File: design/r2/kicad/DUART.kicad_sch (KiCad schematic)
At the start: 17 parts, among them IC4 XR68C681CJTR-F, J1 UART_A, J2 UART_B, J4 Conn_01x06, J7 Conn_01x01_Male, Q1 3.6864MHz

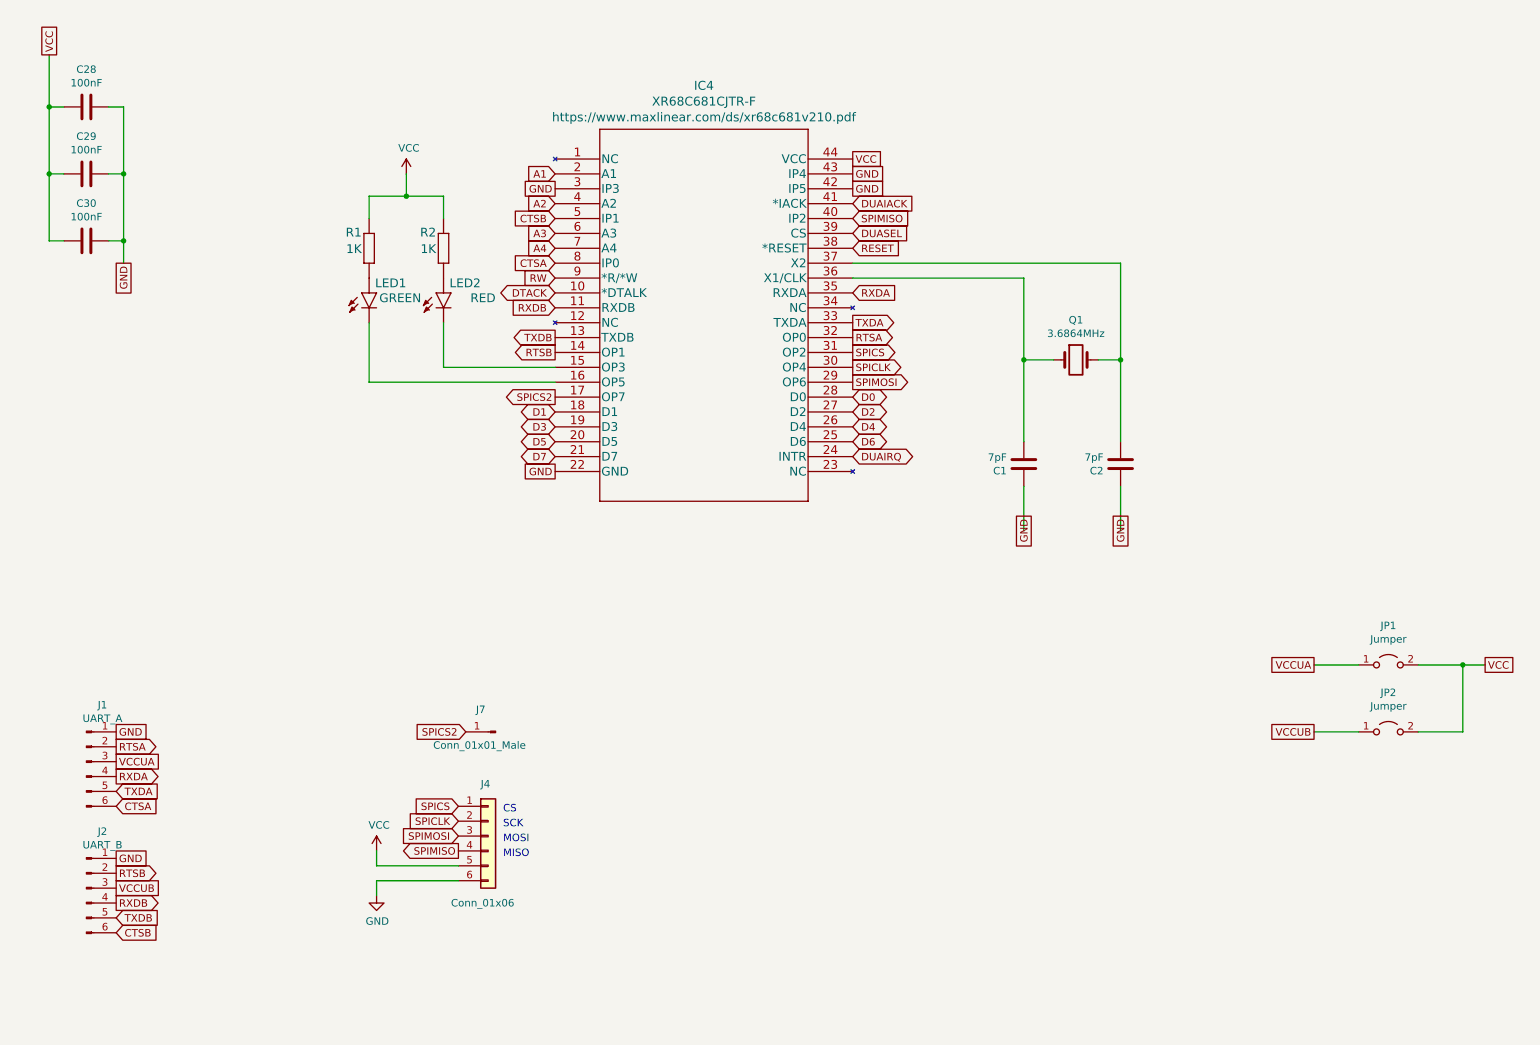
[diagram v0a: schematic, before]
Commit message: Reroute for FTDI
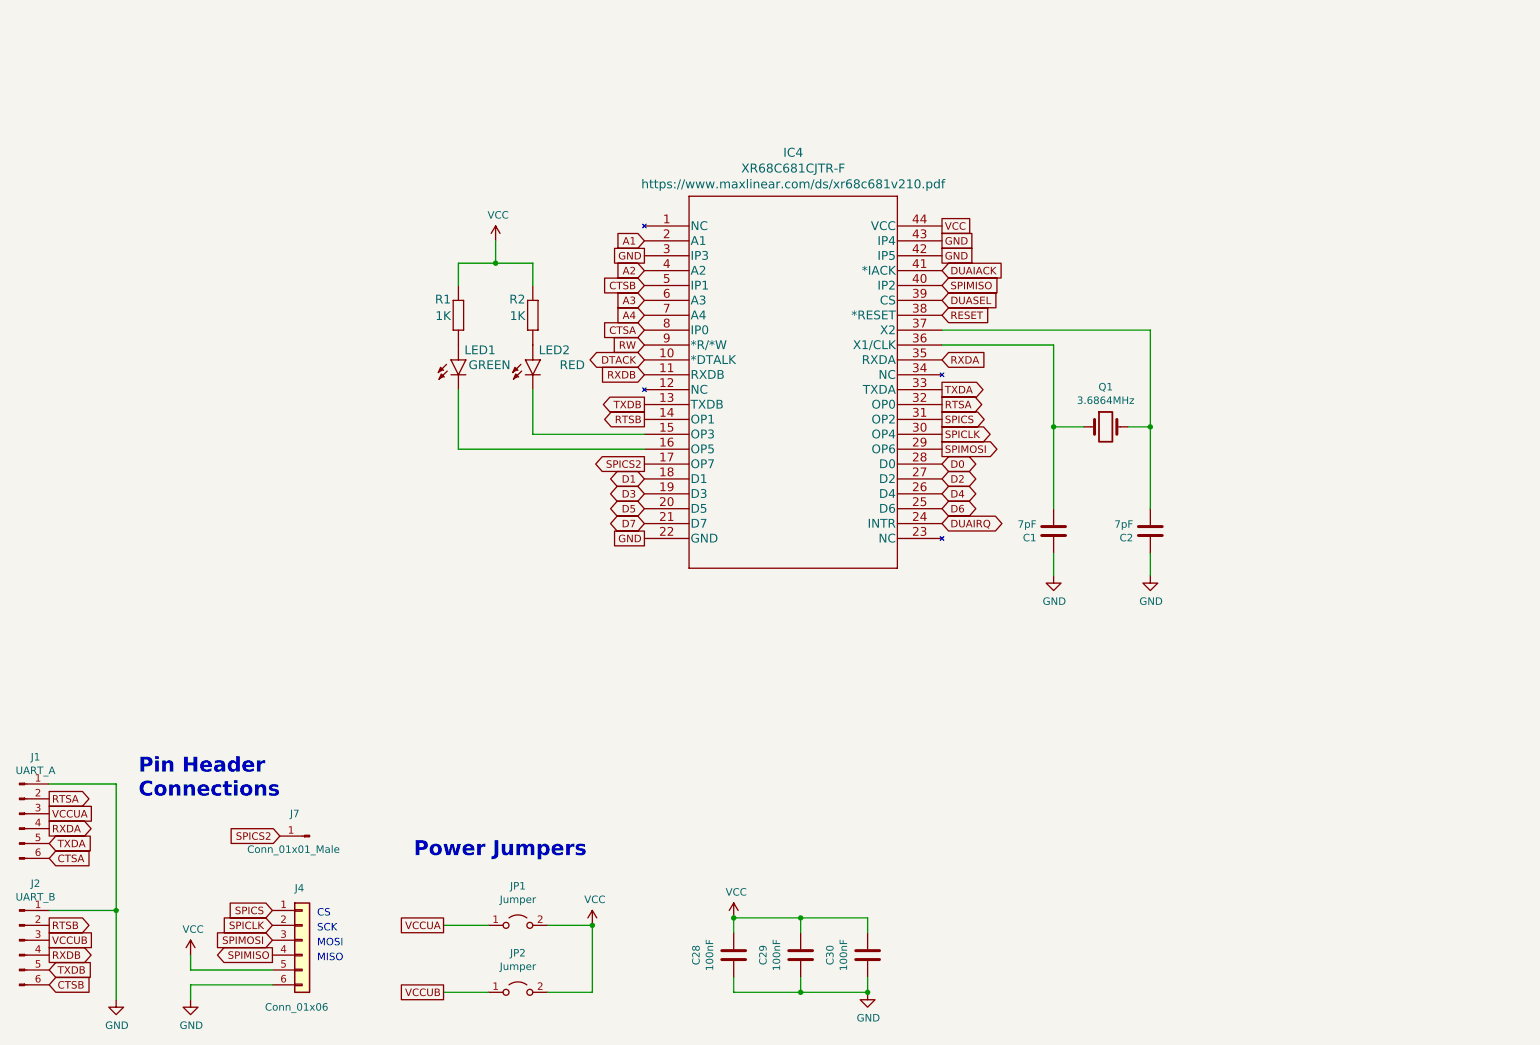
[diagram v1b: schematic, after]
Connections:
- net GND: now also C28.2, C29.2, C30.2; no longer C28.1, C29.1, C30.1
- net VCC: now also C28.1, C29.1, C30.1; no longer C28.2, C29.2, C30.2
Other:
- note added: "Pin Header Connections"
- note added: "Power Jumpers"
- moved on the sheet: C1, C2, C28, C29, C30, IC4, J1, J2, J4, J7, JP1, JP2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
